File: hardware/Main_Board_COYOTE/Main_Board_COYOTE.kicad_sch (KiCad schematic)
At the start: 1 part, among them U1 QRE1113GR

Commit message: Creacion del PCB de sensores QRE1113, y desarrollo del mismo
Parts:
- removed U1: QRE1113GR, OptoDevice:OnSemi_CASE100CY, symbol Sensor_Proximity:QRE1113GR
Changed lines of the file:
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@@
     (comment 1 "Autor: Mauricio Falcon")
-  )
-  (symbol (lib_id "Sensor_Proximity:QRE1113GR") (at 65.3796 72.5424 0) (unit 1)
-    (in_bom yes) (on_board yes) (dnp no) (fields_autoplaced)
-    (property "Reference" "U1" (at 65.3796 64.77 0)
-      (effects (font (size 1.27 1.27)))
-    )
-    (property "Value" "QRE1113GR" (at 65.3796 67.31 0)
-      (effects (font (size 1.27 1.27)))
-    )
-    (property "Footprint" "OptoDevice:OnSemi_CASE100CY" (at 65.3796 77.6224 0)
-      (effects (font (size 1.27 1.27)) hide)
-    )
-    (property "Datasheet" "http://www.onsemi.com/pub/Collateral/QRE1113-D.PDF" (at 65.3796 70.0024 0)
-      (effects (font (size 1.27 1.27)) hide)
-    )
-    (pin "1")
-    (pin "2")
-    (pin "3")
-    (pin "4")
-    (instances
-      (project "Main_Board_COYOTE"
-        (path "/8dc25483-921d-4069-82df-8c37827f2e52"
-          (reference "U1") (unit 1)
-        )
-      )
-    )
   )
   (sheet_instances

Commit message: Creacion del SCH de la main board
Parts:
- added BOOT1, EN1: SW_Push, Button_Switch_THT:SW_PUSH_6mm_H5mm, symbol EESTN5:SW_Push
- added C2, C3: 1uF, Capacitor_SMD:C_0805_2012Metric_Pad1.18x1.45mm_HandSolder, symbol Device:C
- added C3, C4: 1n, EESTN5-v2:C_0805, symbol EESTN5:C
- added J3: FTDI, Connector_PinHeader_2.54mm:PinHeader_1x04_P2.54mm_Horizontal, symbol Connector:Conn_01x04_Pin
- added R1, R3: 470, EESTN5-v2:R_1206, symbol EESTN5:R
- added R2: 1OK, EESTN5-v2:R_1206, symbol EESTN5:R
- added R4: 10K, EESTN5-v2:R_1206, symbol EESTN5:R
- added SW1: SW_SPST, Button_Switch_SMD:SW_SPDT_PCM12, symbol Switch:SW_SPST
- added U2: ESP32-WROOM-32, RF_Module:ESP32-WROOM-32D, symbol RF_Module:ESP32-WROOM-32
- added U2: AMS1117-3.3, Package_TO_SOT_SMD:SOT-223-3_TabPin2, symbol Regulator_Linear:AMS1117-3.3
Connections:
- new net: BOOT1.2, C3.2, R1.1
- new net: C2.1, SW1.2 (B), U2.3 (VI)
- new net: C4.2, EN1.2, R3.1
- new net: U2.1 (GND), U2.15 (GND), U2.38 (GND), U2.39 (GND)
- new net +3.3V: C3.1, J3.2 (Pin_2), U2.2 (VDD), U2.2 (VO)
- new net +3V3: R2.2, R4.2
- new net EN: R3.2, R4.1
- new net GND: BOOT1.1, C2.2, C3.1, C3.2, C4.1, EN1.1, J3.1 (Pin_1), U2.1 (GND)
- new net IO0: R1.2, R2.1
- new net Rx: J3.3 (Pin_3)
- new net Tx: J3.4 (Pin_4)
- new net VBAT: SW1.1 (A)

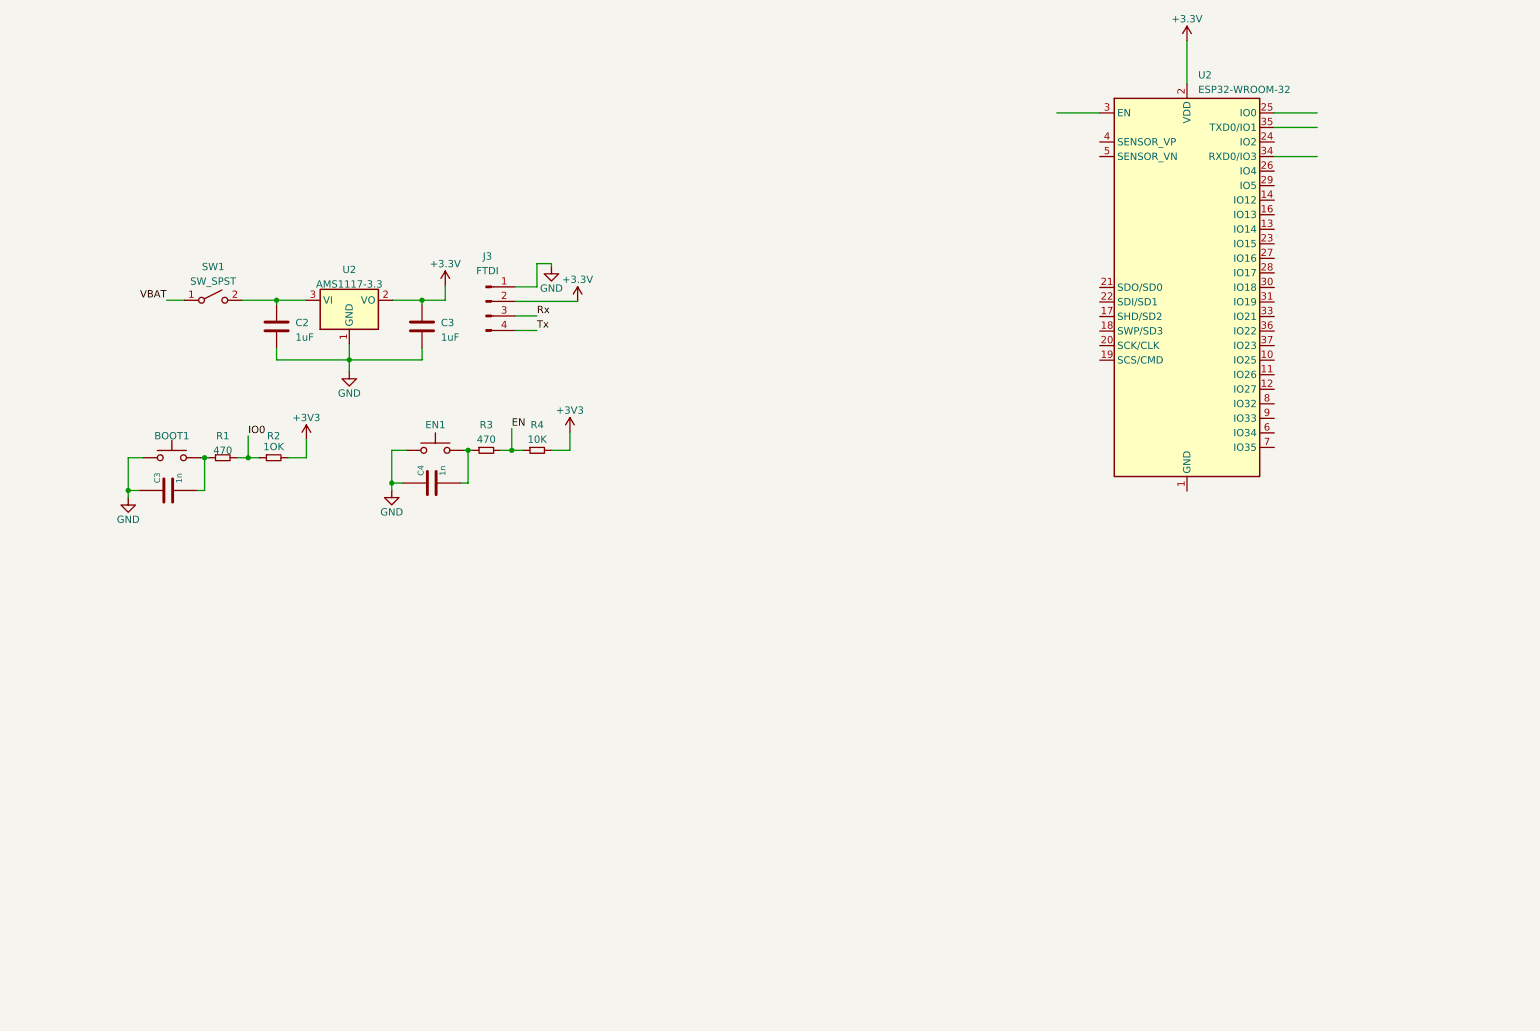
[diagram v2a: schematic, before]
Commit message: Creacion croquis Velocista
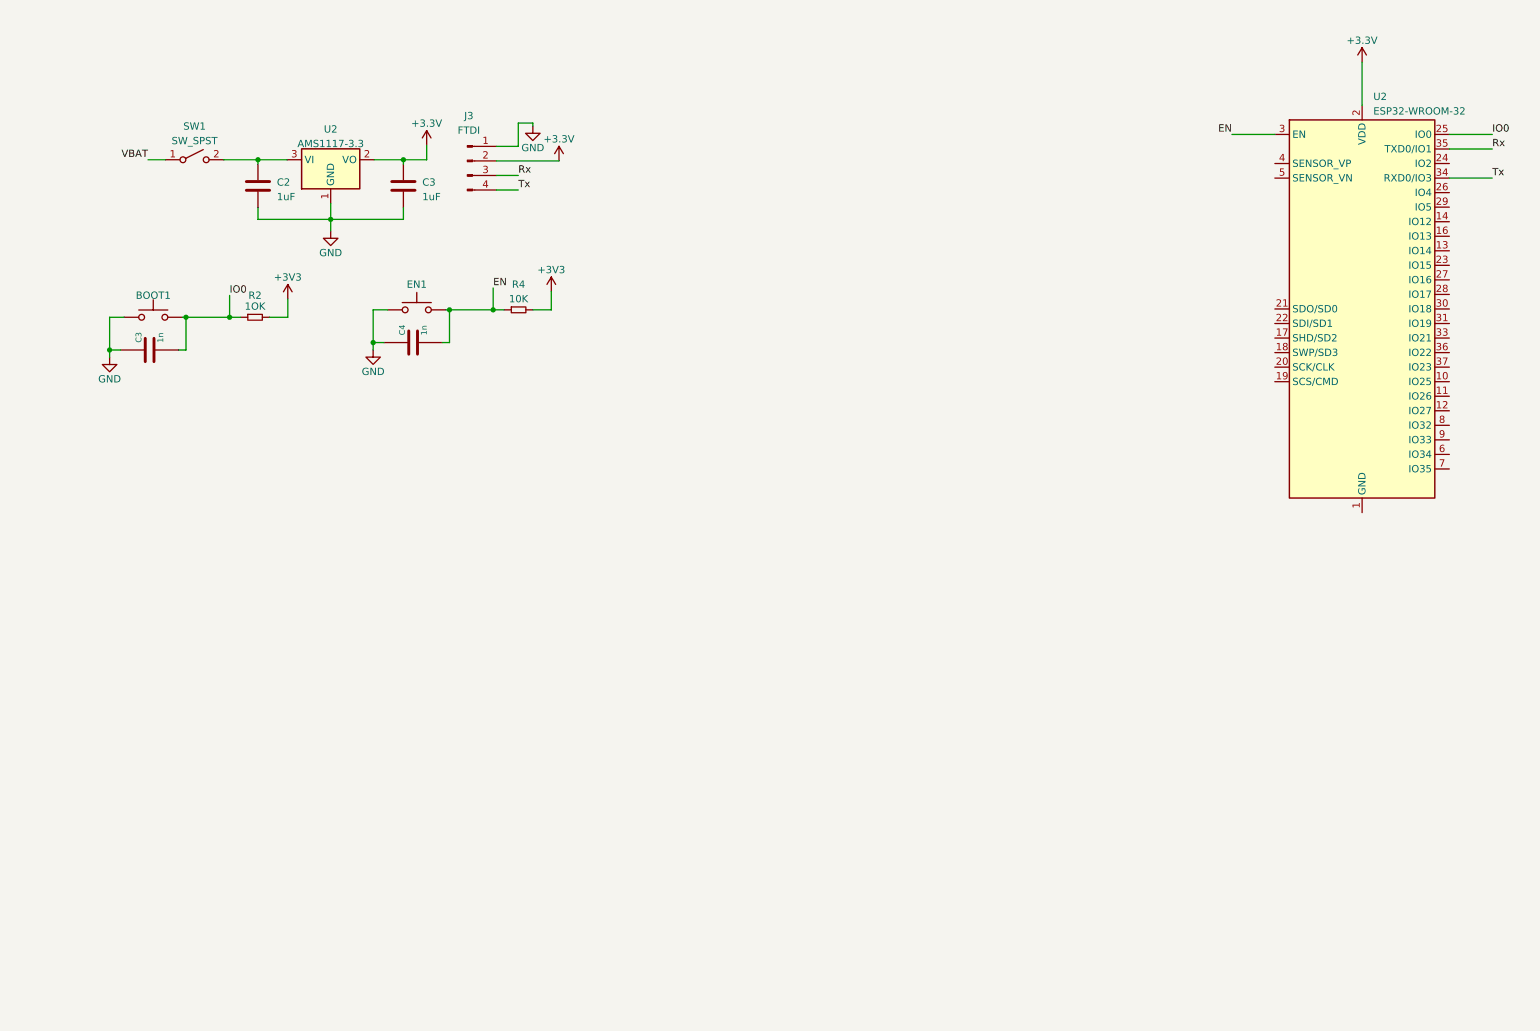
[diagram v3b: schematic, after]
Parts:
- removed R1, R3: 470, EESTN5-v2:R_1206, symbol EESTN5:R
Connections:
- net EN: now also C4.2, EN1.2, U2.3 (EN)
- net IO0: now also BOOT1.2, C3.2, U2.25 (IO0)
- net Rx: now also U2.35 (TXD0/IO1)
- net Tx: now also U2.34 (RXD0/IO3)
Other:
- moved on the sheet: BOOT1, C2, C3, C4, EN1, J3, R2, R4, SW1, U2

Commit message: Creacion finalizacion del croquis velocista
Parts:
- added BZ1: Buzzer, EESTN5-v2:Buzzer_12mm, symbol Device:Buzzer
- added J2, J3: Conn_01x05_Pin, Connector_PinHeader_2.54mm:PinHeader_1x05_P2.54mm_Horizontal, symbol Connector:Conn_01x05_Pin
- added Q1: 2N7002, Package_TO_SOT_SMD:SOT-23, symbol Transistor_FET:2N7002
- added R1, R3: 4K7, EESTN5-v2:R_1206, symbol 2019---Sumo---NANO---BTS7960-rescue:R-EESTN5
- added R3: 10K, EESTN5-v2:R_1206, symbol 2019---Sumo---NANO---BTS7960-rescue:R-EESTN5
- added SW2, SW3: START, Button_Switch_THT:SW_PUSH_6mm_H5mm, symbol 2019---Sumo---NANO---BTS7960-rescue:SW_Push-EESTN5
- added U1: ESP32_DevKit_V1_DOIT, EESTN5-v2:ESP32_DEVKIT_V1_DOIT, symbol EESTN5-v2:ESP32_DevKit_V1_DOIT
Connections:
- net +3.3V is gone; now on net +3V3: C3.1, J3.2 (Pin_2), U2.2 (VDD), U2.2 (VO)
- net +3V3: now also J3.3 (Pin_3), R1.1, R3.1, U1.19 (3V3)
- net GND: now also U2.1 (GND), U2.15 (GND), U2.38 (GND), U2.39 (GND), J2.3 (Pin_3), Q1.2 (S), SW2.1, SW3.1, U1.17 (GND)
- net IO0: no longer U2.25 (IO0)
- net OUT_5: now reaches U2.10 (IO25)
- net OUT_5: now also J2.5 (Pin_5)
- net OUT_6: now reaches U2.11 (IO26)
- net OUT_6: now also J2.4 (Pin_4)
- net OUT_7: now reaches U2.12 (IO27)
- net OUT_7: now also J2.2 (Pin_2)
- net OUT_8: now reaches U2.16 (IO13)
- net OUT_8: now also J2.1 (Pin_1)
- net LED_BUILTING: now reaches U2.24 (IO2)
- net LED_1: now reaches U2.26 (IO4)
- net PUSH_1: now reaches U2.27 (IO16)
- net PUSH_1: now also R1.2, SW2.2, U1.27 (RX2)
- net PUSH_2: now reaches U2.28 (IO17)
- net PUSH_2: now also R3.2, SW3.2, U1.28 (TX2)
- net LED_2: now reaches U2.29 (IO5)
- net BUZZER: now reaches U2.30 (IO18)
- net BUZZER: now also R3.2, U1.30 (IO18)
- net M1A: now reaches U2.31 (IO19)
- net M1A: now also U1.35 (IO22)
- net M1B: now reaches U2.33 (IO21)
- net M1B: now also U1.36 (IO23)
- net M2A: now reaches U2.36 (IO22)
- net M2A: now also U1.31 (IO19)
- net M2B: now reaches U2.37 (IO23)
- net M2B: now also U1.32 (IO21)
- net OUT_1: now reaches U2.6 (IO34)
- net OUT_1: now also J3.5 (Pin_5)
- net OUT_2: now reaches U2.7 (IO35)
- net OUT_2: now also J3.4 (Pin_4)
- net OUT_3: now reaches U2.8 (IO32)
- net OUT_3: now also J3.2 (Pin_2)
- net OUT_4: now reaches U2.9 (IO33)
- net OUT_4: now also J3.1 (Pin_1)
- new net: BZ1.2 (+), Q1.3 (D)
- new net: Q1.1 (G), R3.1
- new net +5V: BZ1.1 (-), U1.18 (VIN)
- new net BOOT: U2.25 (IO0)
- new net SENSOR_1: U1.4 (IO34)
- new net SENSOR_2: U1.5 (IO35)
- new net SENSOR_3: U1.6 (IO32)
- new net SENSOR_4: U1.7 (IO33)
- new net SENSOR_5: U1.8 (IO25)
- new net SENSOR_6: U1.9 (IO26)
- new net SENSOR_7: U1.10 (IO27)
- new net SENSOR_8: U1.13 (IO13)
- no-connect marks 0 -> 18
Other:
- moved on the sheet: BOOT1, C2, C3, C4, EN1, J3, R2, R4, SW1, U2

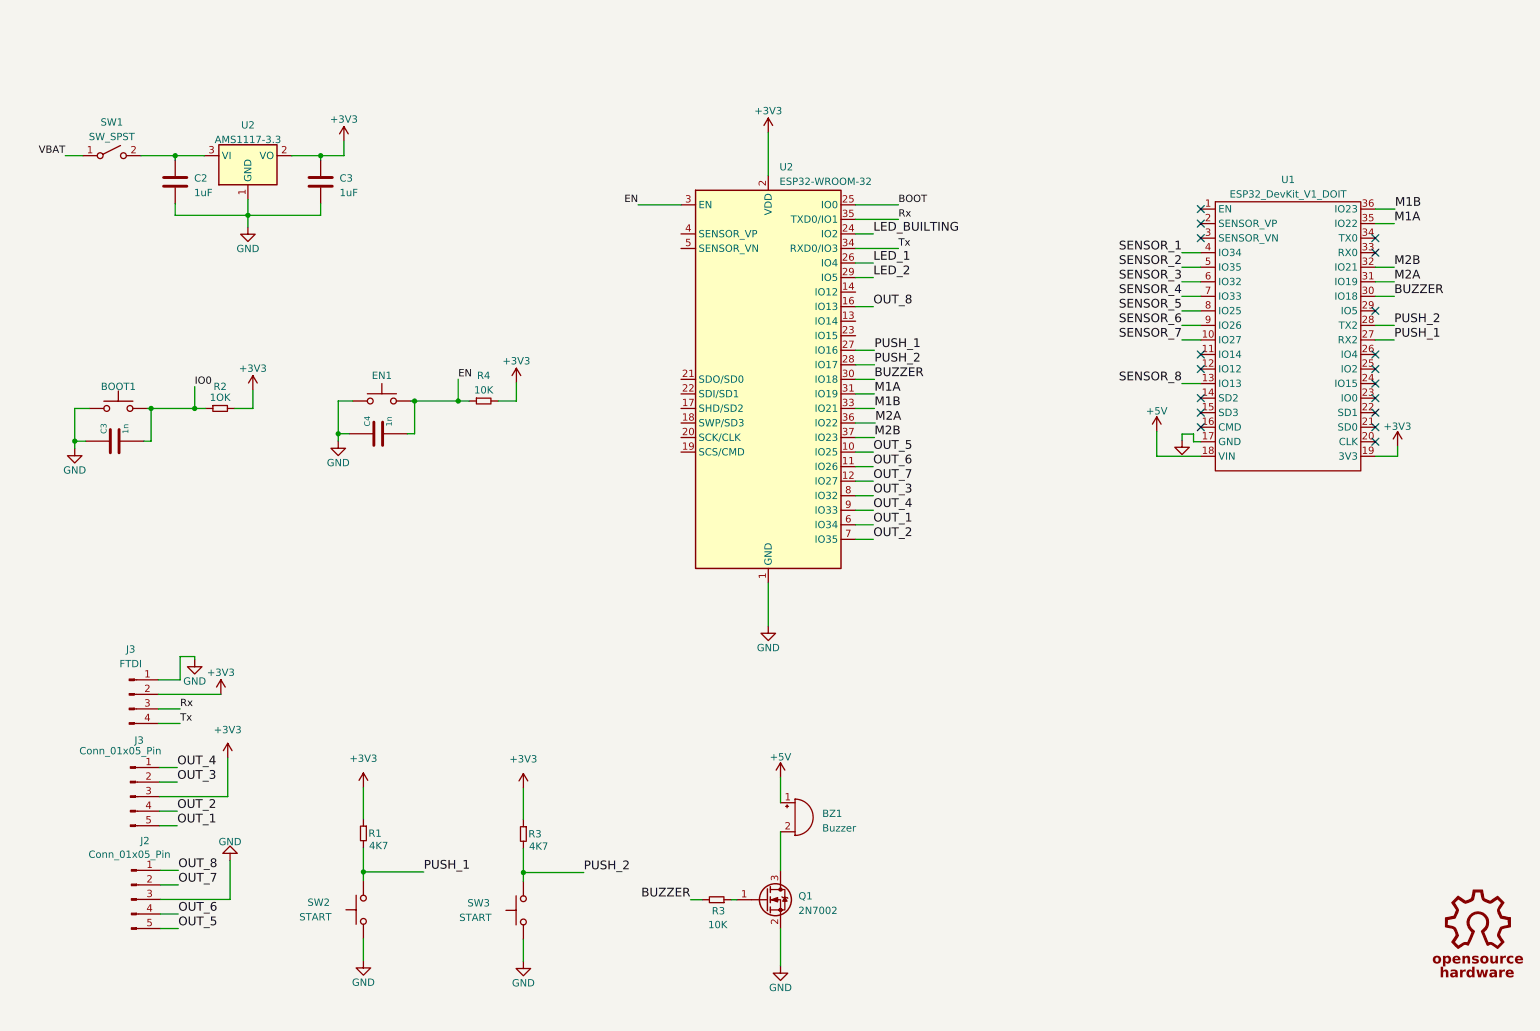
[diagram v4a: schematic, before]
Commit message: Edicion SCh y PCB de la main board
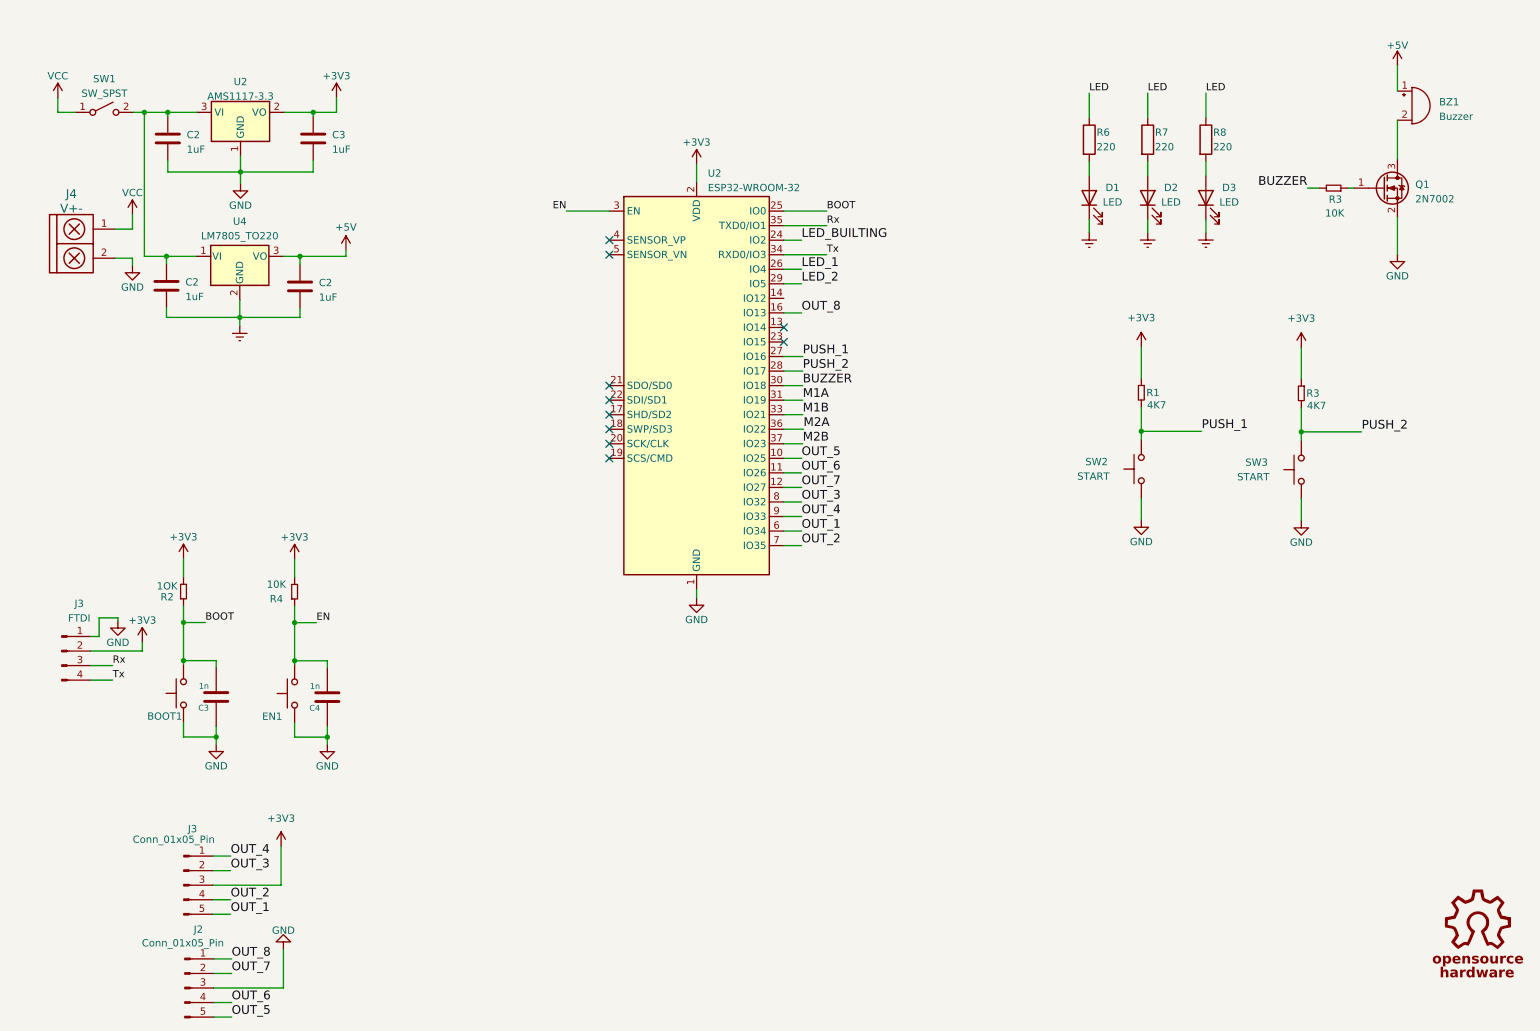
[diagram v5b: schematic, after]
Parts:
- removed U1: ESP32_DevKit_V1_DOIT, EESTN5-v2:ESP32_DEVKIT_V1_DOIT, symbol EESTN5-v2:ESP32_DevKit_V1_DOIT
- added C2 (x2): 1uF, Capacitor_SMD:C_0805_2012Metric_Pad1.18x1.45mm_HandSolder, symbol Device:C
- added D1, D2, D3: LED, LED_THT:LED_D5.0mm, symbol Device:LED
- added J4: V+-, EESTN5-v2:BORNERA2_AZUL, symbol EESTN5-v2:TB_1X2
- added R6, R7, R8: 220, EESTN5-v2:R_1206, symbol Device:R
- added U4: LM7805_TO220, Package_TO_SOT_THT:TO-220-3_Vertical, symbol Regulator_Linear:LM7805_TO220
- SW1: footprint Button_Switch_SMD:SW_SPDT_PCM12 -> EESTN5-v2:SW_SPDT_TH_Vertical
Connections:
- net IO0 is gone; now on net BOOT: BOOT1.2, C3.2, R2.1
- net +5V: now also C2.1, U4.3 (VO)
- net GND: now also J4.2
- net at C2.1, SW1.2 (B), U2.3 (VI): now also C2.1, U4.1 (VI)
- net VBAT renamed VCC
- net VCC: now also J4.1
- new net: D1.2 (A), R6.2
- new net: D3.2 (A), R8.2
- new net: D2.2 (A), R7.2
- new net Earth: C2.2, C2.2, D1.1 (K), D2.1 (K), D3.1 (K), U4.2 (GND)
- new net LED: R6.1, R7.1, R8.1
- no-connect marks 18 -> 10
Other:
- moved on the sheet: BOOT1, BZ1, C2, C3, C4, EN1, J2, J3, Q1, R1, R2, R3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
